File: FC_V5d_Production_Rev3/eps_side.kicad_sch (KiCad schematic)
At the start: 67 parts, among them IC6 LT3652IMSE#PBF, J10 INHIBIT_P2, J11 DF11CZ-12DP-2V(27), J14 Battery Input, J17 Face4 (Z- Face), J19 ISS_INHIBIT, J2 DF11CZ-12DP-2V(27), J20 RBF_Inhibit, J21 Heater Output, J23 Aux Deploy 1, J24 Deploy 2, J29 INHIBIT_S2, J7 INHIBIT_P1, J8 INHIBIT_S1, U10 TPS54226PWPRPWP14_2P31X2P46-L, U13 TPS54225PWPR, U16 INA219AxDCN, U8 INA219AxDCN, U9 MCP23017_SS

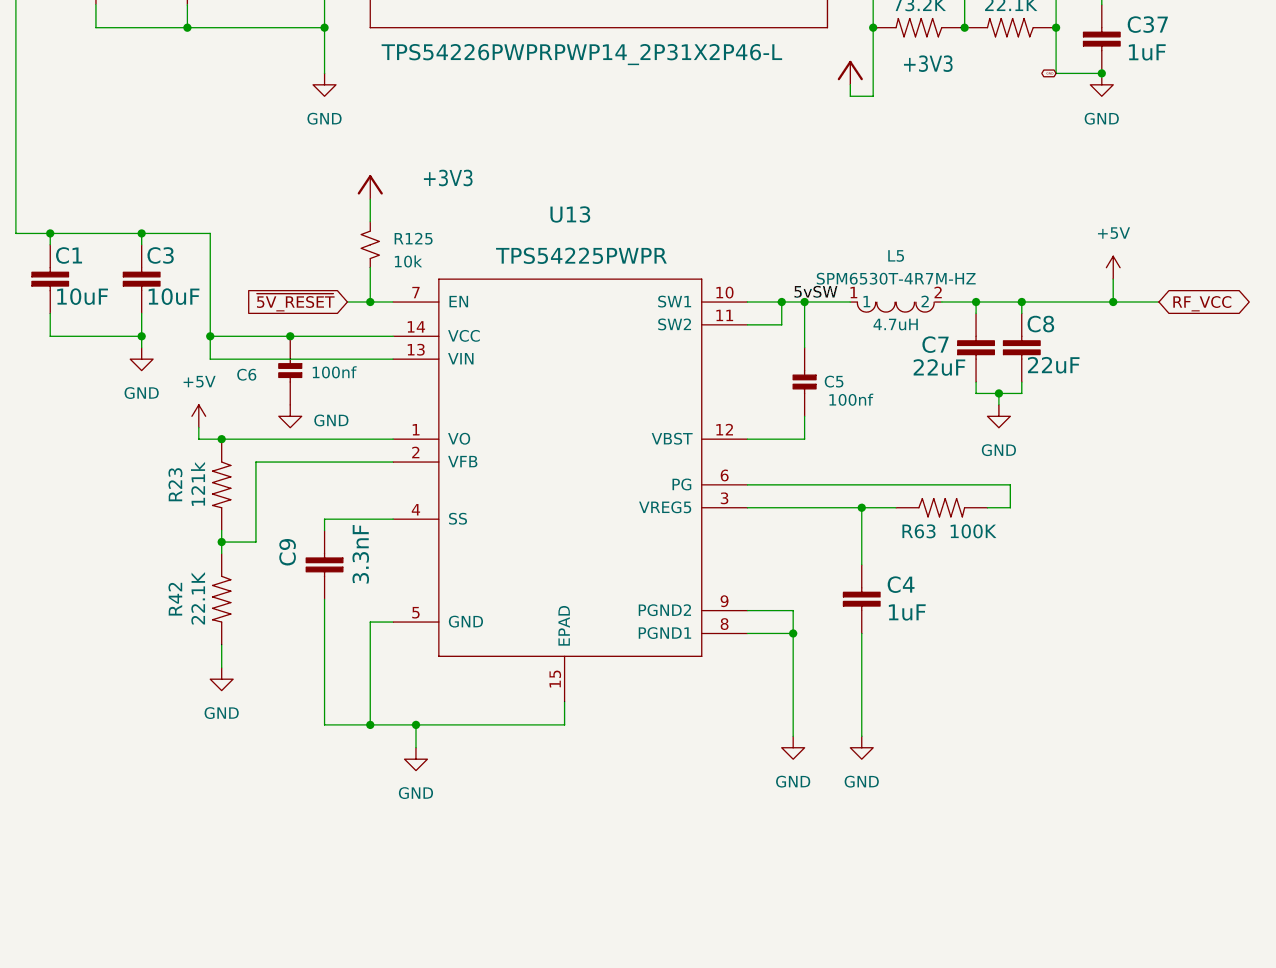
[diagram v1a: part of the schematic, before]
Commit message: Switched 5V Regulator to LT8610
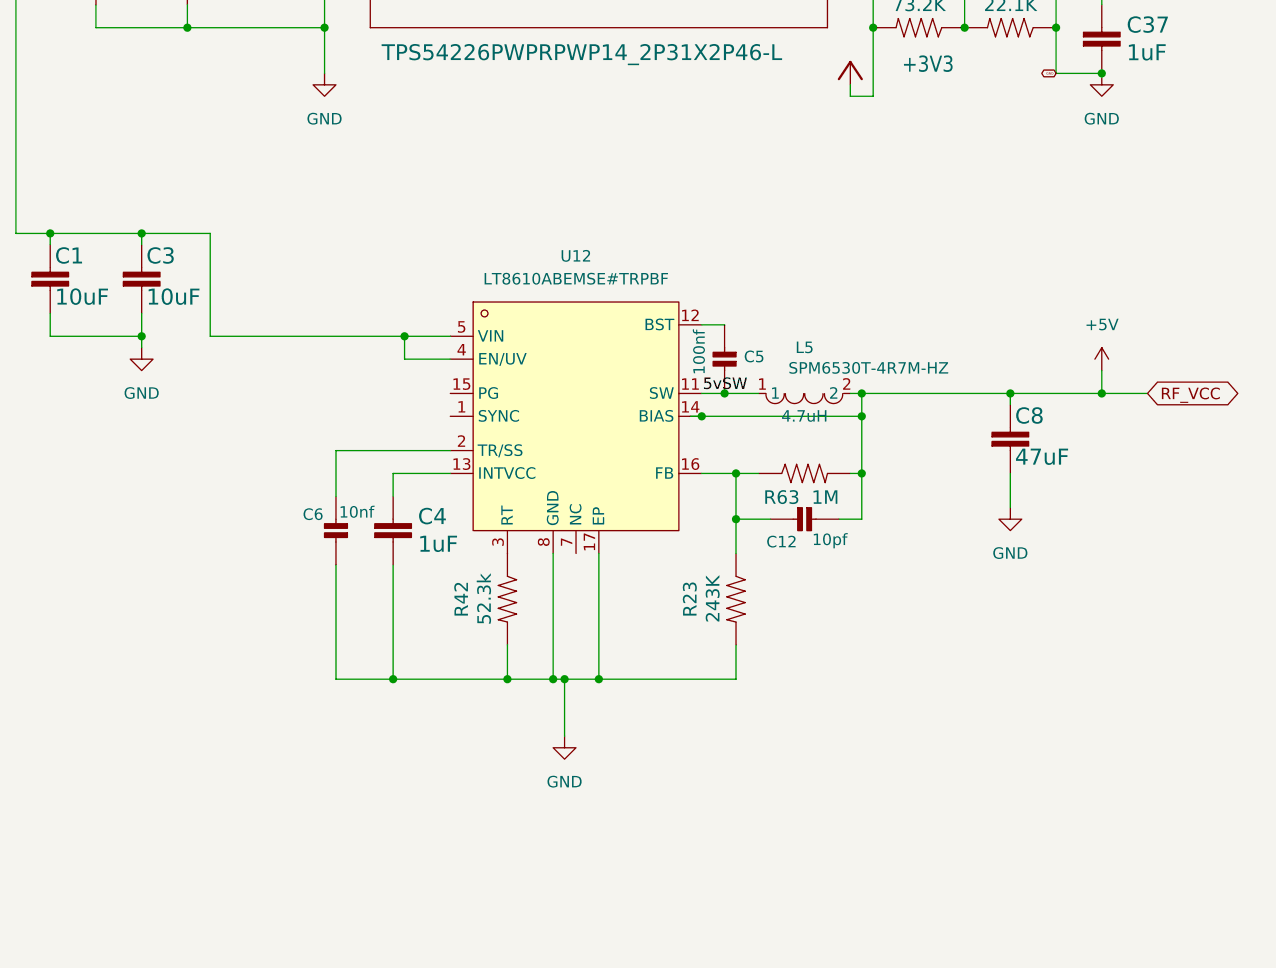
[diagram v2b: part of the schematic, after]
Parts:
- removed C7: 22uF, Capacitor_SMD:C_0603_1608Metric, symbol mainboard:22UF-0805-6.3V-20%
- removed C9: 3.3nF, Capacitor_SMD:C_0603_1608Metric, symbol mainboard:3.3NF-0603-100V-10%
- removed R125: 10k, Resistor_SMD:R_0603_1608Metric, symbol Device:R_Small_US
- removed U13: TPS54225PWPR, MaxLib:PWP14_2P31X2P46-L, symbol mainboard:TPS54226PWPRPWP14_2P31X2P46-L
- added C12: 10pf, Capacitor_SMD:C_0402_1005Metric, symbol Adafruit ItsyBitsy RP2040-eagle-import:CAP_CERAMIC_0402NO
- added U12: LT8610ABEMSE#TRPBF, easyeda2kicad:MSOP-16_L4.0-W3.0-P0.50-LS4.9-BL-EP, symbol easyeda2kicad:LT8610ABEMSE#TRPBF
- C6: value 100nf -> 10nf
- C8: value 22uF -> 47uF; footprint Capacitor_SMD:C_0603_1608Metric -> Capacitor_SMD:C_1210_3225Metric
- R23: value 121k -> 243K
- R42: value 22.1K -> 52.3k
- R63: value 100K -> 1M
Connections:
- net +5V: now also R63.2, C12.1, U12.14 (BIAS); no longer R23.1
- net 5vSW: now also C5.1, U12.10 (SW), U12.11 (SW), U12.9 (SW); no longer C5.2
- net GND: now also R23.2, U12.17 (EP), U12.8 (GND)
- net VBUSP: now also U12.4 (EN/UV), U12.5 (VIN), U12.6 (VIN); no longer C6.2
- net at R42.1: now also U12.3 (RT); no longer R23.2
- net at R63.1: now also R23.1, C12.2, U12.16 (FB); no longer C4.1
- new net: C6.2, U12.2 (TR/SS)
- new net: C5.2, U12.12 (BST)
- new net: C4.1, U12.13 (INTVCC)
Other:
- moved on the sheet: C8

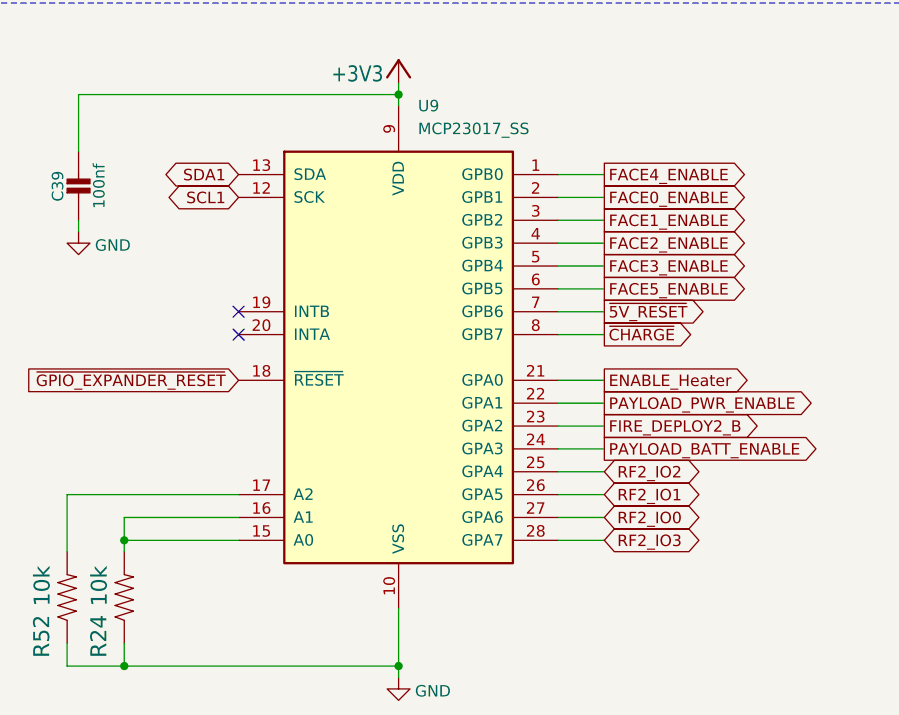
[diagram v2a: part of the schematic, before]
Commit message: Replaced RFM98PW with Ebyte E22-400M30
Also moved MCP GPIO Expander to I2C0 from I2C1.
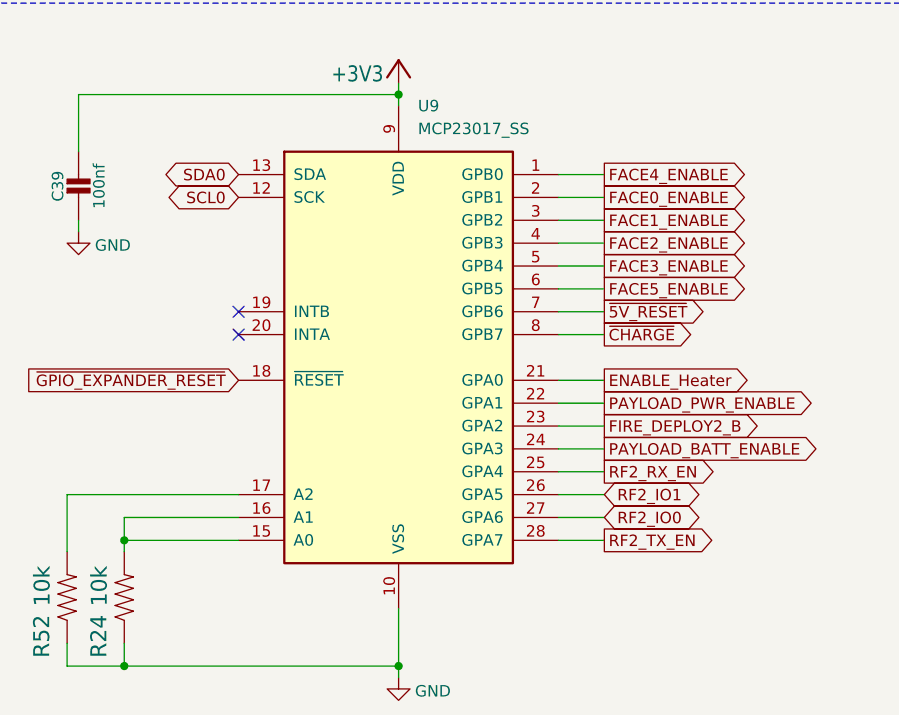
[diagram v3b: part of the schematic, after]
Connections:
- net SCL1 is gone; now on net SCL0: U9.12 (SCK)
- net SDA1 is gone; now on net SDA0: U9.13 (SDA)
- net RF2_IO2 renamed RF2_RX_EN
- net RF2_IO3 renamed RF2_TX_EN
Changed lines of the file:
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@@
-		)
-	)
-	(global_label "RF2_IO1"
-		(shape bidirectional)
-		(at 91.44 260.35 0)
-		(fields_autoplaced yes)
-		(effects
-			(font
-				(size 1.27 1.27)
-			)
-			(justify left)
-		)
-		(property "Intersheetrefs" "${INTERSHEET_REFS}"
-			(at 103.217 260.35 0)
-			(hide yes)
-			(show_name no)
-			(do_not_autoplace no)
-			(effects
-				(font
-					(size 1.27 1.27)
-				)
-				(justify left)
-			)
 		)
 	)
@@
 		(property "Intersheetrefs" "${INTERSHEET_REFS}"
 			(at 365.76 45.6149 90)
+			(hide yes)
+			(show_name no)
+			(do_not_autoplace no)
+			(effects
+				(font
+					(size 1.27 1.27)
+				)
+				(justify left)
+			)
+		)
+	)
+	(global_label "RF2_TX_EN"
+		(shape output)
+		(at 91.44 265.43 0)
+		(fields_autoplaced yes)
+		(effects
+			(font
+				(size 1.27 1.27)
+			)
+			(justify left)
+		)
+		(property "Intersheetrefs" "${INTERSHEET_REFS}"
+			(at 104.5851 265.43 0)
 			(hide yes)
 			(show_name no)
@@
 		)
 	)
+	(global_label "RF2_IO0"
+		(shape bidirectional)
+		(at 91.44 262.89 0)
+		(fields_autoplaced yes)
+		(effects
+			(font
+				(size 1.27 1.27)
+			)
+			(justify left)
+		)
+		(property "Intersheetrefs" "${INTERSHEET_REFS}"
+			(at 103.217 262.89 0)
+			(hide yes)
+			(show_name no)
+			(do_not_autoplace no)
+			(effects
+				(font
+					(size 1.27 1.27)
+				)
+				(justify left)
+			)
+		)
+	)
 	(global_label "FACE3_ENABLE"
 		(shape output)
@@
 		)
 	)
-	(global_label "SDA1"
+	(global_label "SDA0"
 		(shape bidirectional)
 		(at 50.8 224.79 180)
@@
 		)
 		(property "Intersheetrefs" "${INTERSHEET_REFS}"
-			(at 42.0053 224.79 0)
+			(at 41.9259 224.79 0)
 			(hide yes)
 			(show_name no)
@@
 		)
 	)
-	(global_label "RF2_IO0"
-		(shape bidirectional)
-		(at 91.44 262.89 0)
-		(fields_autoplaced yes)
-		(effects
-			(font
-				(size 1.27 1.27)
-			)
-			(justify left)
-		)
-		(property "Intersheetrefs" "${INTERSHEET_REFS}"
-			(at 103.217 262.89 0)
-			(hide yes)
-			(show_name no)
-			(do_not_autoplace no)
-			(effects
-				(font
-					(size 1.27 1.27)
-				)
-				(justify left)
-			)
-		)
-	)
-	(global_label "SCL1"
+	(global_label "SCL0"
 		(shape bidirectional)
 		(at 50.8 227.33 180)
@@
 		)
 		(property "Intersheetrefs" "${INTERSHEET_REFS}"
-			(at 42.0658 227.33 0)
+			(at 41.9864 227.33 0)
 			(hide yes)
 			(show_name no)
@@
 		)
 	)
-	(global_label "RF2_IO2"
-		(shape bidirectional)
+	(global_label "RF2_RX_EN"
+		(shape output)
 		(at 91.44 257.81 0)
 		(fields_autoplaced yes)
@@
 		)
 		(property "Intersheetrefs" "${INTERSHEET_REFS}"
-			(at 103.217 257.81 0)
+			(at 104.8875 257.81 0)
+			(hide yes)
+			(show_name no)
+			(do_not_autoplace no)
+			(effects
+				(font
+					(size 1.27 1.27)
+				)
+				(justify left)
+			)
+		)
+	)
+	(global_label "RF2_IO1"
+		(shape bidirectional)
+		(at 91.44 260.35 0)
+		(fields_autoplaced yes)
+		(effects
+			(font
+				(size 1.27 1.27)
+			)
+			(justify left)
+		)
+		(property "Intersheetrefs" "${INTERSHEET_REFS}"
+			(at 103.217 260.35 0)
 			(hide yes)
 			(show_name no)
@@
 			(hide yes)
 			(show_name no)
-			(do_not_autoplace no)
-			(effects
-				(font
-					(size 1.27 1.27)
-				)
-				(justify left)
-			)
-		)
-	)
-	(global_label "RF2_IO3"
-		(shape bidirectional)
-		(at 91.44 265.43 0)
-		(fields_autoplaced yes)
-		(effects
-			(font
-				(size 1.27 1.27)
-			)
-			(justify left)
-		)
-		(property "Intersheetrefs" "${INTERSHEET_REFS}"
-			(at 103.217 265.43 0)
-			(hide yes)
-			(show_name no)
